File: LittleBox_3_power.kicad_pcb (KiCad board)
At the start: 2 copper layers, 69 parts, among them P10 CONN_01X03, P13 CONN_01X03, P16 CONN_01X03, P17 CONN_01X03, P18 CONN_01X01, P19 CONN_01X03, P20 CONN_01X01, P21 CONN_01X01, P3 CONN_01X01, P4 CONN_01X01, P400IN+1 CONN_1, P400IN-1 CONN_1, P9 CONN_01X03, Q1 C3M0065090D, Q10 IPW6045CP, Q2 C3M0065090D, Q3 C3M0065090D, Q4 C3M0065090D, Q5 C3M0065090D, Q6 C3M0065090D, Q7 IPW6045CP, Q8 IPW6045CP, Q9 IPW6045CP, U18 ACS712, U19 ACS712, U21 ACS712, U23 ACS712, U5 ACS712, U6 ACS712

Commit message: Last mods
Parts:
- removed C2: 100n, Capacitors_SMD:C_0603
- removed R24: 1, Resistors_SMD:R_0603
- added ?: , inverter:hole_3mm, F.Cu at (110.5, 93.0)
- added ? (x2): , inverter:hole_3mm, F.Cu at (241.3, 48.7)
- added ?: , inverter:hole_3mm, F.Cu at (241.3, 99.1)
- added ?: , inverter:hole_3mm, F.Cu at (95.5, 88.7)
- added ?: , inverter:hole_3mm, F.Cu at (112.8, 47.8)
- added ?: , inverter:hole_3mm, F.Cu at (156.5, 95.8)
- added ?: , inverter:hole_3mm, F.Cu at (156.5, 54.7)
- added ?: , inverter:hole_3mm, F.Cu at (94.5, 43.6)
- added ?: , inverter:hole_3mm, F.Cu at (141.2, 100.6)
- added ?: , inverter:hole_3mm, F.Cu at (141.2, 50.2)
- added ?: , inverter:hole_3mm, F.Cu at (170.9, 100.6)
- added ?: , inverter:hole_3mm, F.Cu at (170.9, 51.0)
- added ?: , inverter:hole_3mm, F.Cu at (223.5, 48.7)
- added ?: , inverter:hole_3mm, F.Cu at (223.5, 99.1)
- added P23: CONN_01X02, inverter:Pin_Header_Straight_1x02_round, F.Cu at (115.5, 69.8)
- added P24: CONN_01X02, inverter:Pin_Header_Straight_1x02_round, F.Cu at (89.0, 67.3)
- added P25: CONN_01X02, inverter:Pin_Header_Straight_1x02_round, F.Cu at (136.5, 73.8)
- added P26: CONN_01X02, inverter:Pin_Header_Straight_1x02_round, F.Cu at (146.0, 77.3)
- added P27: CONN_01X02, inverter:Pin_Header_Straight_1x02_round, F.Cu at (166.0, 69.3)
- added P28: CONN_01X03, inverter:Pin_Header_Straight_1x03_round, F.Cu at (177.0, 77.8)
- added P29: CONN_01X02, inverter:Pin_Header_Straight_1x02_round, F.Cu at (218.8, 67.8)
- added P30: CONN_01X03, inverter:Pin_Header_Straight_1x03_round, F.Cu at (229.0, 80.3)
- added P31: CONN_01X02, inverter:Pin_Header_Straight_1x02_round, F.Cu at (236.5, 71.8)
- added P32: CONN_01X03, inverter:Pin_Header_Straight_1x03_round, F.Cu at (246.5, 80.3)
- added PI2C_2: CONN_01X05, inverter:Header_1x5_metric, F.Cu at (81.5, 72.1)
- added PI2C_22: CONN_01X05, Pin_Headers:Pin_Header_Straight_1x05, F.Cu at (78.2, 66.7)
- added R11: 1k, Resistors_SMD:R_0603, F.Cu at (92.7, 59.5)
- added R18: 1k, Resistors_SMD:R_0603, F.Cu at (150.5, 76.8)
- added R19: 1k, Resistors_SMD:R_0603, F.Cu at (131.6, 69.9)
- added R21: 1k, Resistors_SMD:R_0603, F.Cu at (180.1, 80.6)
- added R25: 1k, Resistors_SMD:R_0603, F.Cu at (213.9, 76.5)
- added R28: 1k, Resistors_SMD:R_0603, F.Cu at (213.6, 70.9)
- added R30: 1k, Resistors_SMD:R_0603, F.Cu at (232.5, 76.3)
- added R34: 1k, Resistors_SMD:R_0603, F.Cu at (239.0, 74.3)
- added R9: 1k, Resistors_SMD:R_0603, F.Cu at (110.7, 76.5)
- C4, C47, C5, C9: value 0.1u -> 100n
- U23, U6: footprint Housings_SOIC:SOIC-8_3.9x4.9mm_Pitch1.27mm -> inverter:ACS712
- moved R23 5.08 mm to (168.4, 66.9)
- moved U23 2.36 mm to (220.5, 61.9), turned to 0 degrees
- moved C39 2.34 mm to (218.6, 56.3)
- moved U5 2.24 mm to (139.1, 87.2)
- moved C38 2.20 mm to (222.0, 56.3)
- moved C4 1.68 mm to (141.1, 92.5)
- moved C5 1.47 mm to (137.7, 92.5)
- moved C36 1.44 mm to (255.1, 73.3)
- moved C37 1.44 mm to (251.7, 73.3)
- moved U6 1.15 mm to (142.5, 62.3), turned to 0 degrees
- moved C34 0.94 mm to (251.8, 70.8)
- moved C19 0.91 mm to (255.0, 70.8)
- moved C43 0.47 mm to (92.7, 50.9)
- moved C47 0.29 mm to (145.1, 56.5), turned to 0 degrees
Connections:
- net /M_I175 renamed Net-(P10-Pad2)
- net /M_I225 renamed Net-(P9-Pad2)
- net /M_IOUT2 renamed Net-(P17-Pad2)
- net /PB2 renamed Net-(P16-Pad2)
- net GND_P renamed GND_12
- net VCC3_A renamed VCC5_A
- P13 pad 2: /M_IOUT1 -> Net-(P13-Pad2)
- P19 pad 2: /M_IOUT1 -> Net-(P19-Pad2)
- U18 pad 7: /M_IOUT1 -> Net-(P19-Pad2)
- U23 pad 7: /M_IOUT1 -> Net-(P13-Pad2)
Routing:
- net GND_12: track 283.8 -> 308.9 mm, vias 0 -> 1
- net Net-(P30-Pad1): track 0.00 -> 21.1 mm, vias 0 -> 1
- net Net-(C13-Pad1): track 24.4 -> 45.3 mm
- net Net-(C32-Pad1): track 42.5 -> 63.3 mm
- net V175: track 6.87 -> 26.6 mm
- net /B1: track 102.4 -> 121.0 mm
- net Net-(P32-Pad1): track 0.00 -> 17.8 mm, vias 0 -> 1
- net /M_IOUT1: track 14.5 -> 0.00 mm
- net Net-(C21-Pad1): track 23.2 -> 32.3 mm
- net Net-(P19-Pad2): track 0.00 -> 8.26 mm, vias 0 -> 1
- net Net-(P23-Pad1): track 0.00 -> 7.06 mm
- net Net-(P13-Pad2): track 0.00 -> 7.00 mm, vias 0 -> 1
- net Net-(P24-Pad1): track 0.00 -> 6.96 mm
- net Net-(P27-Pad1): track 0.00 -> 6.59 mm
- net VCC5_A: track 50.5 -> 56.6 mm, vias 0 -> 1
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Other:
- board outline added: 200 x 70 mm
- net class 10A: clearance 0.3 -> 0.8
- net class 5A: clearance 0.3 -> 0.8
- net class Default: clearance 0.2 -> 0.25
- rule trace_clearance: 0.2 -> 0.25

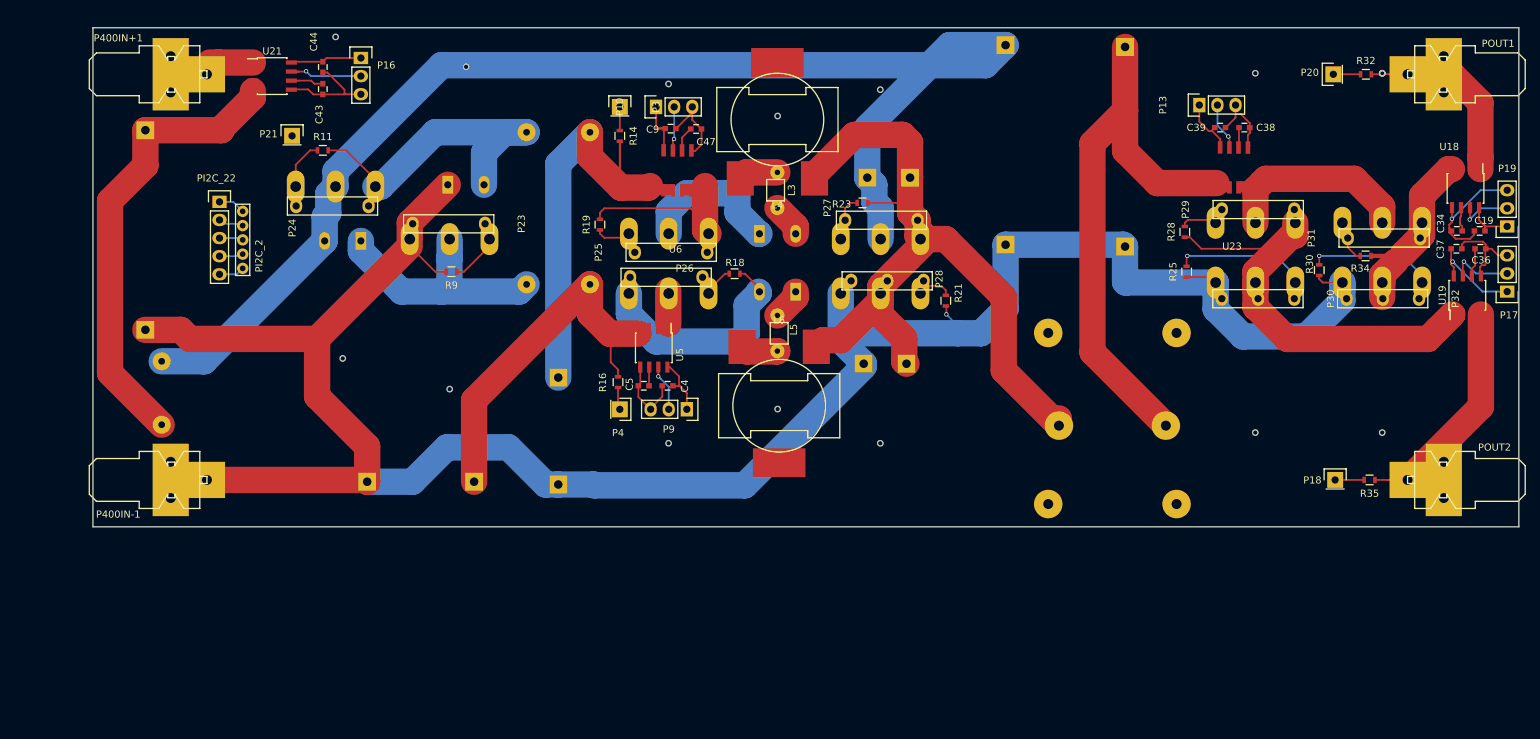
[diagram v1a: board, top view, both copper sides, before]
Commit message: Check high voltage spacings and modify accordingly
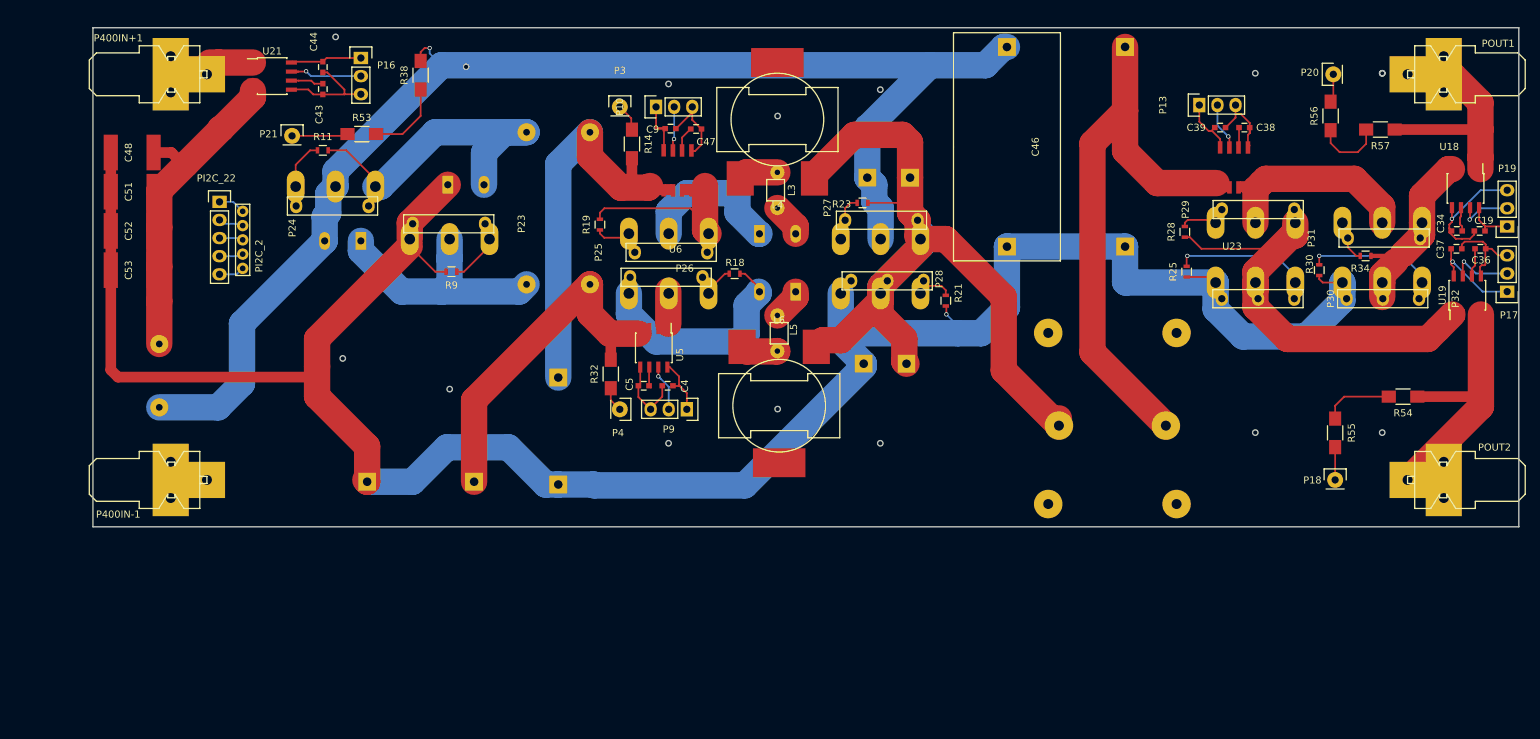
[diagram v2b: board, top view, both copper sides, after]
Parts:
- removed the ? at (241.3, 48.7) (x2)
- removed R16, R35: 4.7M, Resistors_SMD:R_0603
- added ? (x2): , inverter:hole_3mm, F.Cu at (241.3, 48.7)
- added C51: 1uF 630V, inverter:6050_MLCC, F.Cu at (66.0, 65.3)
- added C52: 1uF 630V, inverter:6050_MLCC, F.Cu at (66.0, 70.8)
- added C53: 1uF 630V, inverter:6050_MLCC, F.Cu at (66.0, 76.3)
- added R38: 2.2M, Resistors_SMD:R_1206_HandSoldering, F.Cu at (106.4, 49.0)
- added R53: 2.2M, Resistors_SMD:R_1206_HandSoldering, F.Cu at (98.2, 57.2)
- added R54: 2.2M, Resistors_SMD:R_1206_HandSoldering, F.Cu at (244.2, 94.1)
- added R55: 2.2M, Resistors_SMD:R_1206_HandSoldering, F.Cu at (234.7, 99.1)
- added R56: 2.2M, Resistors_SMD:R_1206_HandSoldering, F.Cu at (234.1, 54.7)
- added R57: 2.2M, Resistors_SMD:R_1206_HandSoldering, F.Cu at (241.0, 56.6)
- C46: moved to F.Cu
- C48: footprint inverter:C_Rect_W15_L32_P27.5 -> inverter:6050_MLCC; moved to F.Cu
- P3: footprint Socket_Strips:Socket_Strip_Straight_1x01 -> inverter:Pin_Header_Straight_1x01_round
- R14, R32: value 4.7M -> 2.2M; footprint Resistors_SMD:R_0603 -> Resistors_SMD:R_1206_HandSoldering
- moved R32 114.0 mm to (133.1, 90.9), turned to 90 degrees
- moved C48 11.0 mm to (66.0, 59.8), turned to 270 degrees
- moved L9 2.46 mm to (69.8, 91.1), turned to 180 degrees
- moved R14 2.04 mm to (136.1, 58.6)
- moved C46 0.33 mm to (188.7, 59.0)
- turned P3 to 0 degrees
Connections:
- R32 pad 1: /PB0 -> /PA6
- R32 pad 2: Net-(POUT1-Pad1) -> Net-(C7-Pad1)
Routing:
- net Net-(C48-Pad2): track 64.3 -> 49.1 mm
- net GND_12: track 308.9 -> 322.0 mm
- net Net-(R38-Pad1): track 0.00 -> 11.0 mm
- net Net-(R54-Pad2): track 0.00 -> 9.86 mm
- net Net-(R56-Pad1): track 0.00 -> 9.81 mm
- net /M_VIN: track 0.00 -> 7.88 mm
- net Net-(C8-Pad1): track 63.6 -> 55.8 mm
- net Net-(POUT1-Pad1): track 26.3 -> 33.2 mm
- net Net-(POUT2-Pad1): track 32.1 -> 37.0 mm
- net Net-(C7-Pad1): track 53.7 -> 50.2 mm
- net V400+: track 182.2 -> 184.3 mm, vias 0 -> 1
- net /PA6: track 3.17 -> 3.84 mm
- net /PA1: track 3.31 -> 3.90 mm
- net /PB1: track 4.08 -> 4.60 mm

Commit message: gerber generation
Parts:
- removed the ? at (110.5, 93.0)
- removed the ? at (241.3, 48.7) (x2)
- removed the ? at (241.3, 99.1)
- removed the ? at (95.5, 88.7)
- removed the ? at (112.8, 47.8)
- removed the ? at (156.5, 95.8)
- removed the ? at (156.5, 54.7)
- removed the ? at (94.5, 43.6)
- removed the ? at (141.2, 100.6)
- removed the ? at (141.2, 50.2)
- removed the ? at (170.9, 100.6)
- removed the ? at (170.9, 51.0)
- removed the ? at (223.5, 48.7)
- removed the ? at (223.5, 99.1)
- added ?: , inverter:hole_3mm, F.Cu at (100.0, 110.7)
- added ? (x2): , inverter:hole_3mm, F.Cu at (230.8, 66.4)
- added ?: , inverter:hole_3mm, F.Cu at (230.8, 116.8)
- added ?: , inverter:hole_3mm, F.Cu at (85.0, 106.4)
- added ?: , inverter:hole_3mm, F.Cu at (102.3, 65.5)
- added ?: , inverter:hole_3mm, F.Cu at (146.0, 113.5)
- added ?: , inverter:hole_3mm, F.Cu at (146.0, 72.4)
- added ?: , inverter:hole_3mm, F.Cu at (84.0, 61.3)
- added ?: , inverter:hole_3mm, F.Cu at (130.7, 118.3)
- added ?: , inverter:hole_3mm, F.Cu at (130.7, 67.9)
- added ?: , inverter:hole_3mm, F.Cu at (160.4, 118.3)
- added ?: , inverter:hole_3mm, F.Cu at (160.4, 68.7)
- added ?: , inverter:hole_3mm, F.Cu at (213.0, 66.4)
- added ?: , inverter:hole_3mm, F.Cu at (213.0, 116.8)
- added FID1: Fiducial_1mm_Dia_2.54mm_Outer_CopperTop, Fiducials:Fiducial_1mm_Dia_2.54mm_Outer_CopperTop, F.Cu at (55.0, 55.0)
- added FID2: Fiducial_1mm_Dia_2.54mm_Outer_CopperTop, Fiducials:Fiducial_1mm_Dia_2.54mm_Outer_CopperTop, F.Cu at (55.0, 135.0)
- added FID3: Fiducial_1mm_Dia_2.54mm_Outer_CopperTop, Fiducials:Fiducial_1mm_Dia_2.54mm_Outer_CopperTop, F.Cu at (245.0, 55.0)
- C48, C51, C52, C53: footprint inverter:6050_MLCC -> inverter:MLCC_SuperCap_5750_BackCu
- L7: value 1.2m -> 1.2mH
- moved C53 22.1 mm to (55.2, 95.6), turned to 0 degrees
- moved C52 22.0 mm to (55.2, 89.9), turned to 0 degrees
- moved C51 21.6 mm to (55.2, 84.0), turned to 0 degrees
- moved C48 21.3 mm to (55.2, 78.1), turned to 0 degrees
- moved P17 20.6 mm to (248.4, 97.0)
- moved P19 20.6 mm to (248.4, 87.9)
- moved R21 20.6 mm to (169.6, 98.3)
- moved U6 20.6 mm to (132.0, 80.0)
- moved C5 20.6 mm to (127.3, 110.2)
- moved C9 20.6 mm to (131.0, 74.2)
- moved P25 20.6 mm to (126.0, 91.5)
- moved P3 20.6 mm to (123.9, 71.1)
- moved P4 20.6 mm to (123.9, 113.5)
- moved U21 20.6 mm to (75.1, 66.8)
- moved R53 20.6 mm to (87.7, 74.9)
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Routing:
- net Net-(C48-Pad2): track 49.1 -> 72.1 mm, vias 0 -> 4
- net GND_12: track 322.0 -> 343.7 mm, vias 1 -> 2
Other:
- board size 200 x 70 mm -> 200 x 90 mm

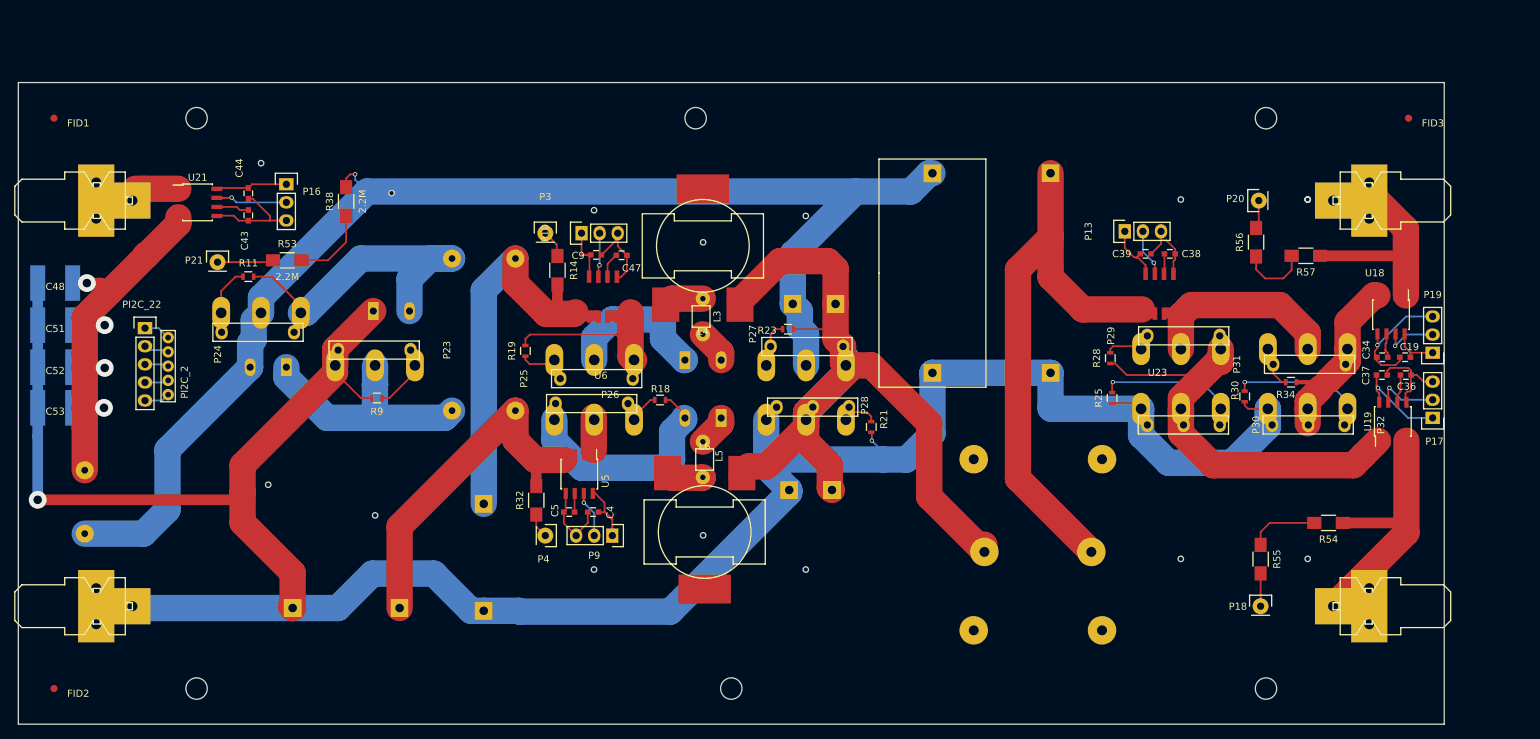
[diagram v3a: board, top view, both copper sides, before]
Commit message: Deplacement des fiducials et de l'origine afin d'avoir des coordonees positives
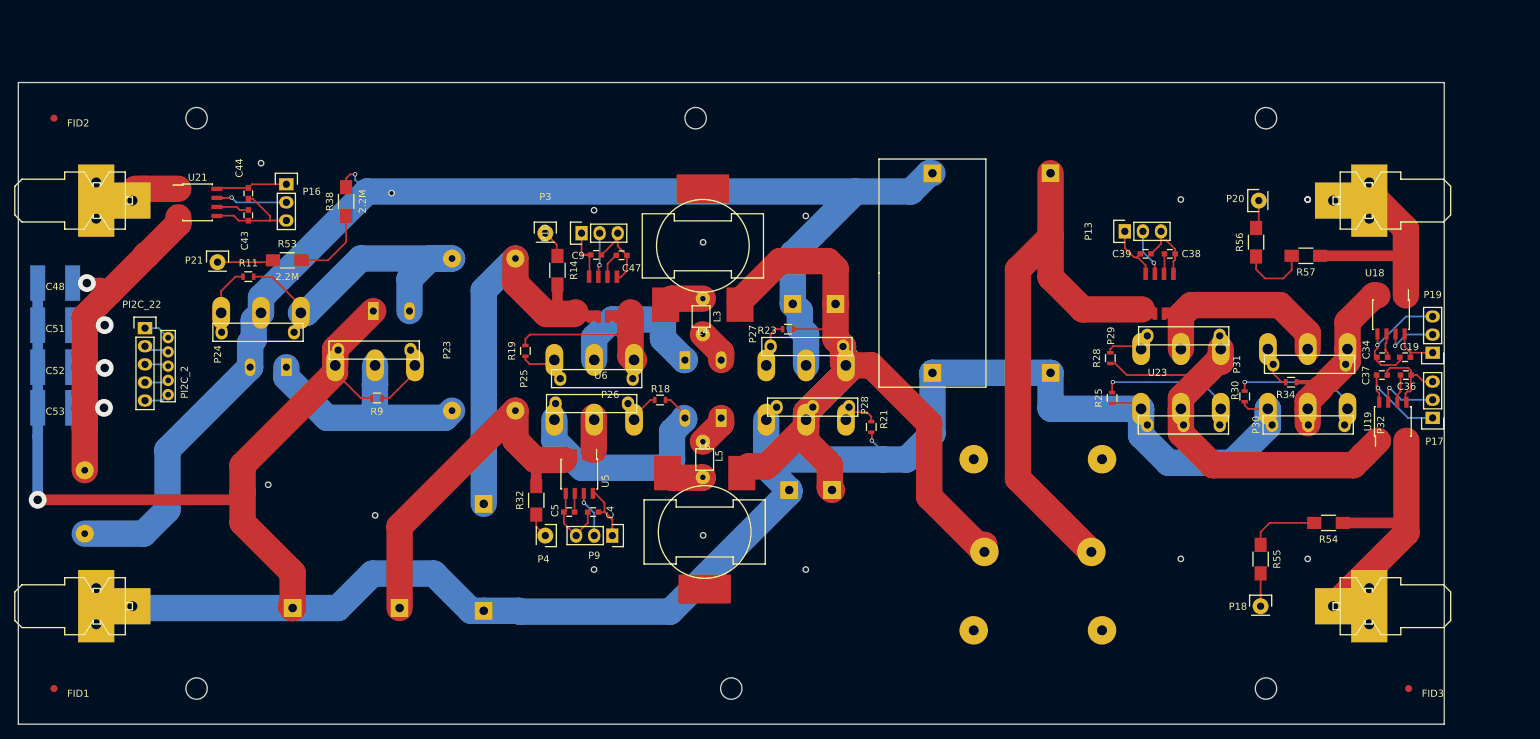
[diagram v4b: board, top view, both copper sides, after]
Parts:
- removed the ? at (230.8, 66.4) (x2)
- added ? (x2): , inverter:hole_3mm, F.Cu at (230.8, 66.4)
- moved FID1 80.0 mm to (55.0, 135.0)
- moved FID2 80.0 mm to (55.0, 55.0)
- moved FID3 80.0 mm to (245.0, 135.0)
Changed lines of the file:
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@@
     (pad_to_mask_clearance 0)
     (pad_to_paste_clearance -0.07)
-    (aux_axis_origin 55 55)
-    (grid_origin 55 55)
+    (aux_axis_origin 55 135)
+    (grid_origin 55 135)
     (visible_elements 7FFFFF7F)
     (pcbplotparams
@@
   )
   (module Fiducials:Fiducial_1mm_Dia_2.54mm_Outer_CopperTop (layer F.Cu)
+    (at 55 135)
+    (descr "Circular Fiducial, 1mm bare copper top; 2.54mm keepout")
+    (tags marker)
+    (attr virtual)
+    (fp_text reference FID1 (at 3.4 0.7) (layer F.SilkS)
+      (effects (font (size 1 1) (thickness 0.15)))
+    )
+    (fp_text value Fiducial_1mm_Dia_2.54mm_Outer_CopperTop (at 0 -1.8) (layer F.Fab)
+      (effects (font (size 1 1) (thickness 0.15)))
+    )
+    (fp_circle (center 0 0) (end 1.55 0) (layer F.CrtYd) (width 0.05))
+    (pad ~ smd circle (at 0 0) (size 1 1) (layers F.Cu F.Mask)
+      (solder_mask_margin 0.77) (clearance 0.77))
+  )
+  (module Fiducials:Fiducial_1mm_Dia_2.54mm_Outer_CopperTop (layer F.Cu)
     (at 55 55)
     (descr "Circular Fiducial, 1mm bare copper top; 2.54mm keepout")
     (tags marker)
     (attr virtual)
-    (fp_text reference FID1 (at 3.4 0.7) (layer F.SilkS)
+    (fp_text reference FID2 (at 3.4 0.7) (layer F.SilkS)
       (effects (font (size 1 1) (thickness 0.15)))
     )
@@
   )
   (module Fiducials:Fiducial_1mm_Dia_2.54mm_Outer_CopperTop (layer F.Cu)
-    (at 55 135)
+    (at 245 135)
     (descr "Circular Fiducial, 1mm bare copper top; 2.54mm keepout")
     (tags marker)
-    (attr virtual)
-    (fp_text reference FID2 (at 3.4 0.7) (layer F.SilkS)
-      (effects (font (size 1 1) (thickness 0.15)))
-    )
-    (fp_text value Fiducial_1mm_Dia_2.54mm_Outer_CopperTop (at 0 -1.8) (layer F.Fab)
-      (effects (font (size 1 1) (thickness 0.15)))
-    )
-    (fp_circle (center 0 0) (end 1.55 0) (layer F.CrtYd) (width 0.05))
-    (pad ~ smd circle (at 0 0) (size 1 1) (layers F.Cu F.Mask)
-      (solder_mask_margin 0.77) (clearance 0.77))
-  )
-  (module Fiducials:Fiducial_1mm_Dia_2.54mm_Outer_CopperTop (layer F.Cu)
-    (at 245 55)
-    (descr "Circular Fiducial, 1mm bare copper top; 2.54mm keepout")
-    (tags marker)
